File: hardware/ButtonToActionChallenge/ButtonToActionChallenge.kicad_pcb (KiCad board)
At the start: 2 copper layers, 27.4 x 17.3 mm, 4 parts, among them J1 ActionOutput, J2 Button Wires, J3 ActionOutput, J4 ActionTrigger

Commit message: adding vias to a couple of PCBs, magic wand PCB changes
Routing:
- net GND: vias 2 -> 8
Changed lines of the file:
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@@
   (segment (start 152.4 77.978) (end 156.972 73.406) (width 0.762) (layer "F.Cu") (net 2))
   (via (at 142.494 75.438) (size 0.8) (drill 0.4) (layers "F.Cu" "B.Cu") (free) (net 3))
+  (via (at 156.8 81.5) (size 0.8) (drill 0.4) (layers "F.Cu" "B.Cu") (free) (net 3))
   (via (at 148.844 72.898) (size 0.8) (drill 0.4) (layers "F.Cu" "B.Cu") (free) (net 3))
+  (via (at 143.4 68.8) (size 0.8) (drill 0.4) (layers "F.Cu" "B.Cu") (free) (net 3))
+  (via (at 156.5 77) (size 0.8) (drill 0.4) (layers "F.Cu" "B.Cu") (free) (net 3))
+  (via (at 143.4 80.1) (size 0.8) (drill 0.4) (layers "F.Cu" "B.Cu") (free) (net 3))
+  (via (at 159.2 67.6) (size 0.8) (drill 0.4) (layers "F.Cu" "B.Cu") (free) (net 3))
+  (via (at 148.8 80.2) (size 0.8) (drill 0.4) (layers "F.Cu" "B.Cu") (free) (net 3))
   (segment (start 146.812 74.89) (end 149.9 77.978) (width 0.508) (layer "F.Cu") (net 4))
   (segment (start 146.812 74.676) (end 146.812 74.89) (width 0.508) (layer "F.Cu") (net 4))

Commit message: updating button to action challenge PCB to use 12v for button LED
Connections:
- J2 pad 3: +5V -> +12V
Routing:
- net +12V: track 28.6 -> 38.1 mm
- net +5V: track 50.0 -> 50.6 mm
- net GND: vias 8 -> 13
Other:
- board text added: "Action Challenge Connector V2"
- board text removed: "Action Challenge Connector V1"

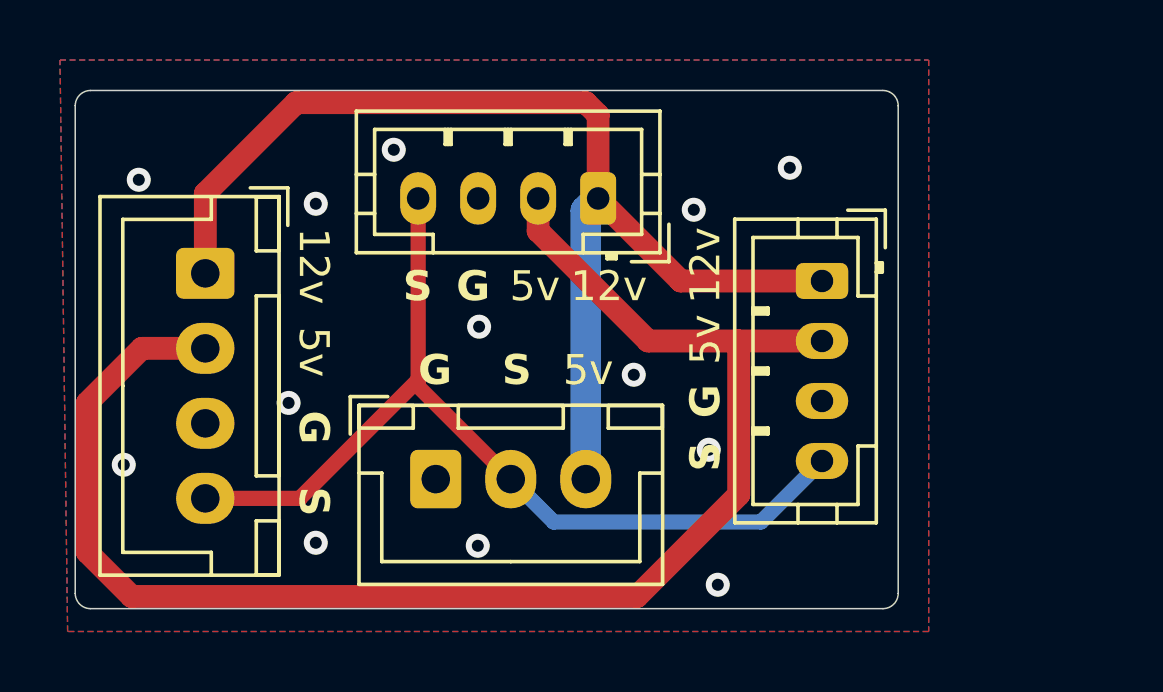
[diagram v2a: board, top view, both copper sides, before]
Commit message: Updated Action Challenge Connector Board
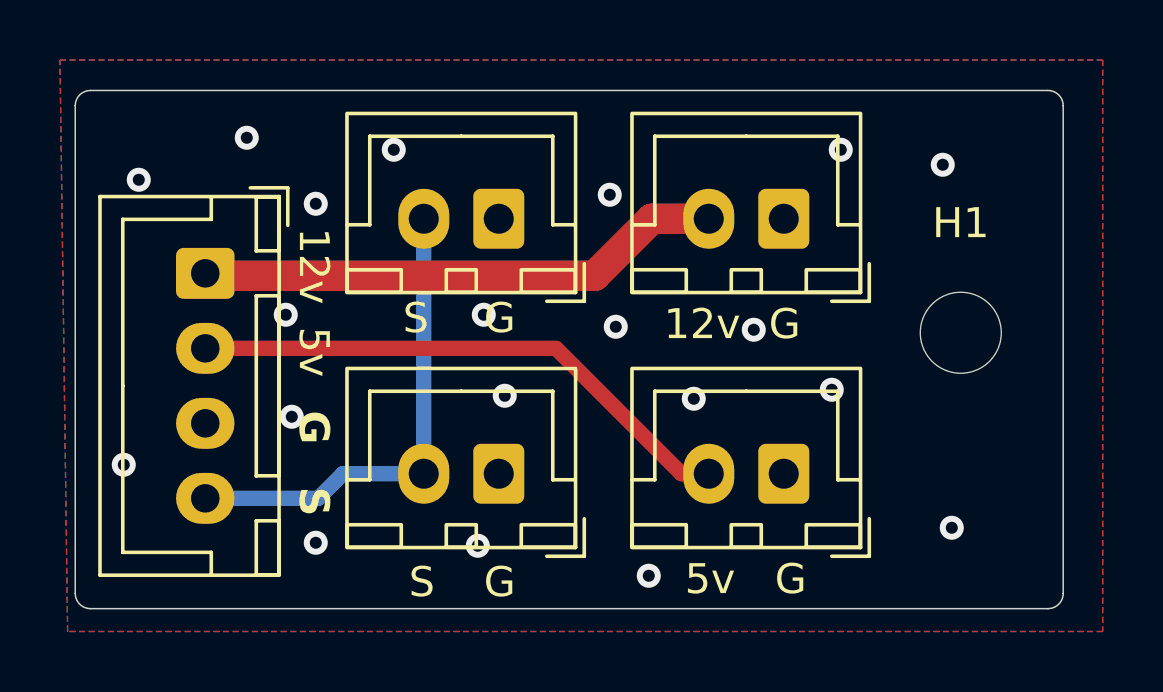
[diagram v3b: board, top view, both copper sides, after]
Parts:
- removed J4: ActionTrigger, Connector_JST:JST_PH_B4B-PH-K_1x04_P2.00mm_Vertical
- added H1: MountingHole, MountingHole:MountingHole_2.7mm_M2.5, F.Cu at (164.9, 73.1)
- added J5: Action Switch 1, Connector_JST:JST_XH_B2B-XH-A_1x02_P2.50mm_Vertical, F.Cu at (149.5, 69.3)
- added J6: Action Switch 2, Connector_JST:JST_XH_B2B-XH-A_1x02_P2.50mm_Vertical, F.Cu at (149.5, 77.8)
- J1: value ActionOutput -> 5v Connector; footprint Connector_JST:JST_PH_B4B-PH-K_1x04_P2.00mm_Vertical -> Connector_JST:JST_XH_B2B-XH-A_1x02_P2.50mm_Vertical
- J2: value Button Wires -> 12v Connector; footprint Connector_JST:JST_XH_B3B-XH-A_1x03_P2.50mm_Vertical -> Connector_JST:JST_XH_B2B-XH-A_1x02_P2.50mm_Vertical
- moved J2 14.5 mm to (159.0, 69.3), turned to 180 degrees
- moved J1 11.1 mm to (159.0, 77.8)
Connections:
- J1 pad 1: +12V -> GND
- J2 pad 2: ActionSignal -> +12V
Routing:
- net +5V: track 50.6 -> 18.5 mm
- net +12V: track 38.1 -> 17.6 mm
- net ActionSignal: track 31.2 -> 16.1 mm
- net GND: vias 13 -> 20
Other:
- board size 27.4 x 17.3 mm -> 32.9 x 17.3 mm
- board text added: "Action Challenge Connector V3"
- board text removed: "Action Challenge Connector V2"
